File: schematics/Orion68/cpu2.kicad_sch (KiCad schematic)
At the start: 37 parts, among them J10 Conn_02x08_Counter_Clockwise, J600 Euro96pin, J601 clock, J602 clock1, Q5 2N3904, Q6 2N3904, SW1 sw_reset, U16 74LS139, U21 74LS20, U22 74HC164, U24 74HC4078, U600 68000D, U601 74LS393, U602 74HC74, U603 74HC14, U604 ATmega8-16P

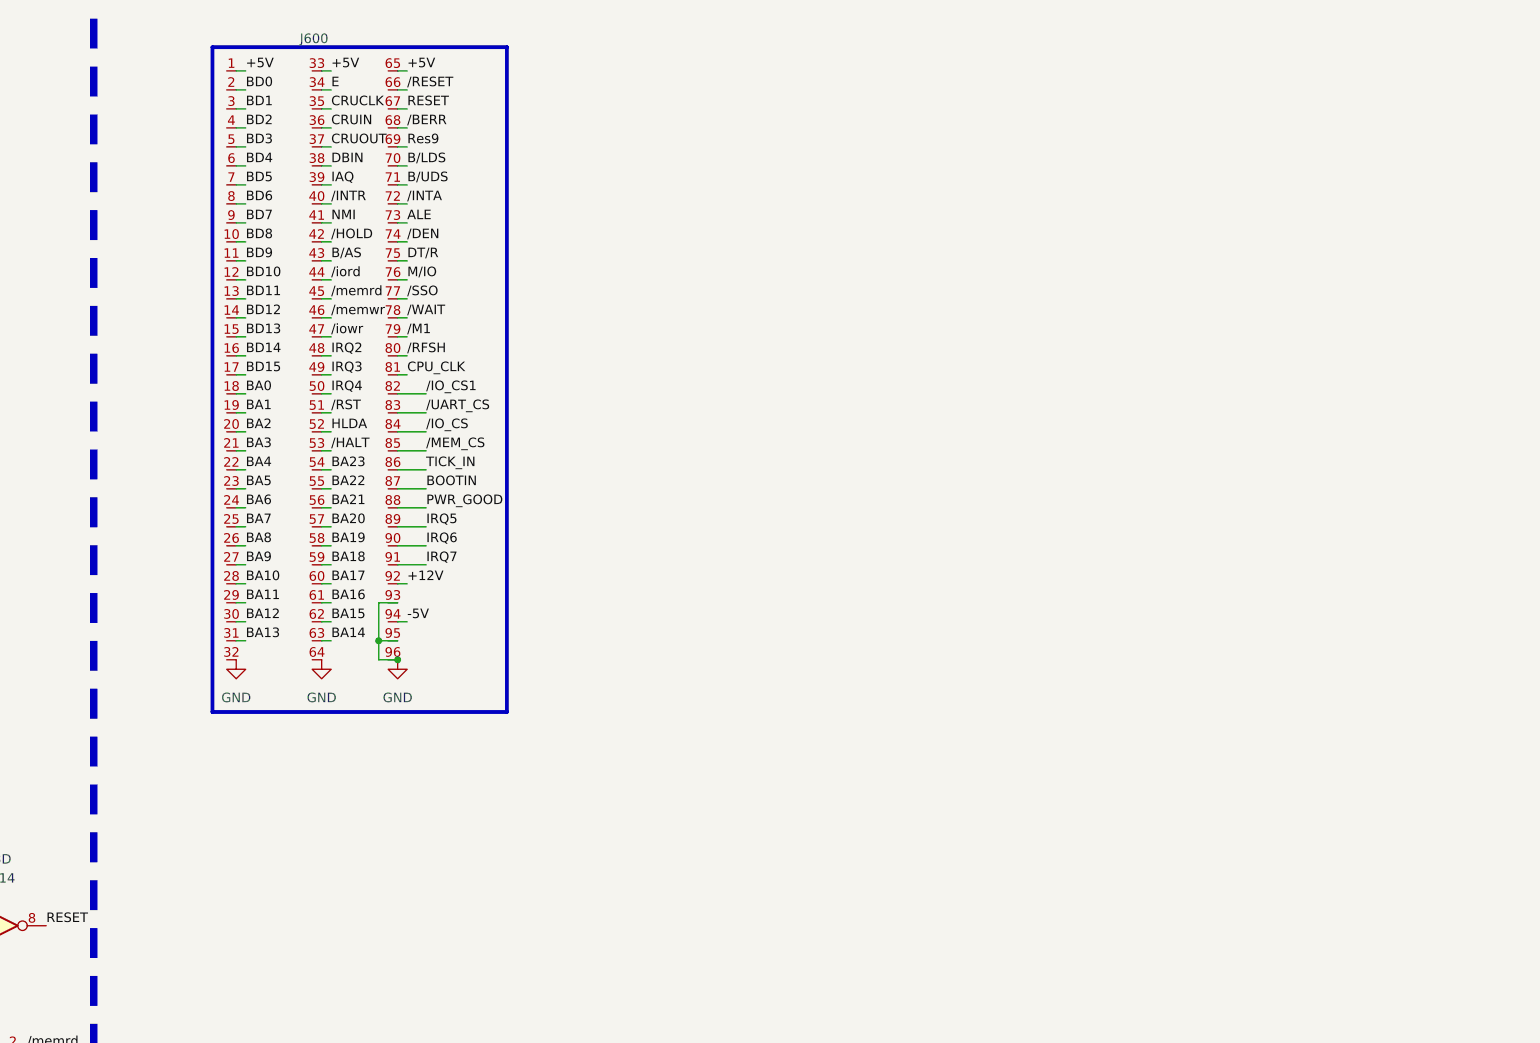
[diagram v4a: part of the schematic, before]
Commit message: B column DIN conn. all in GND
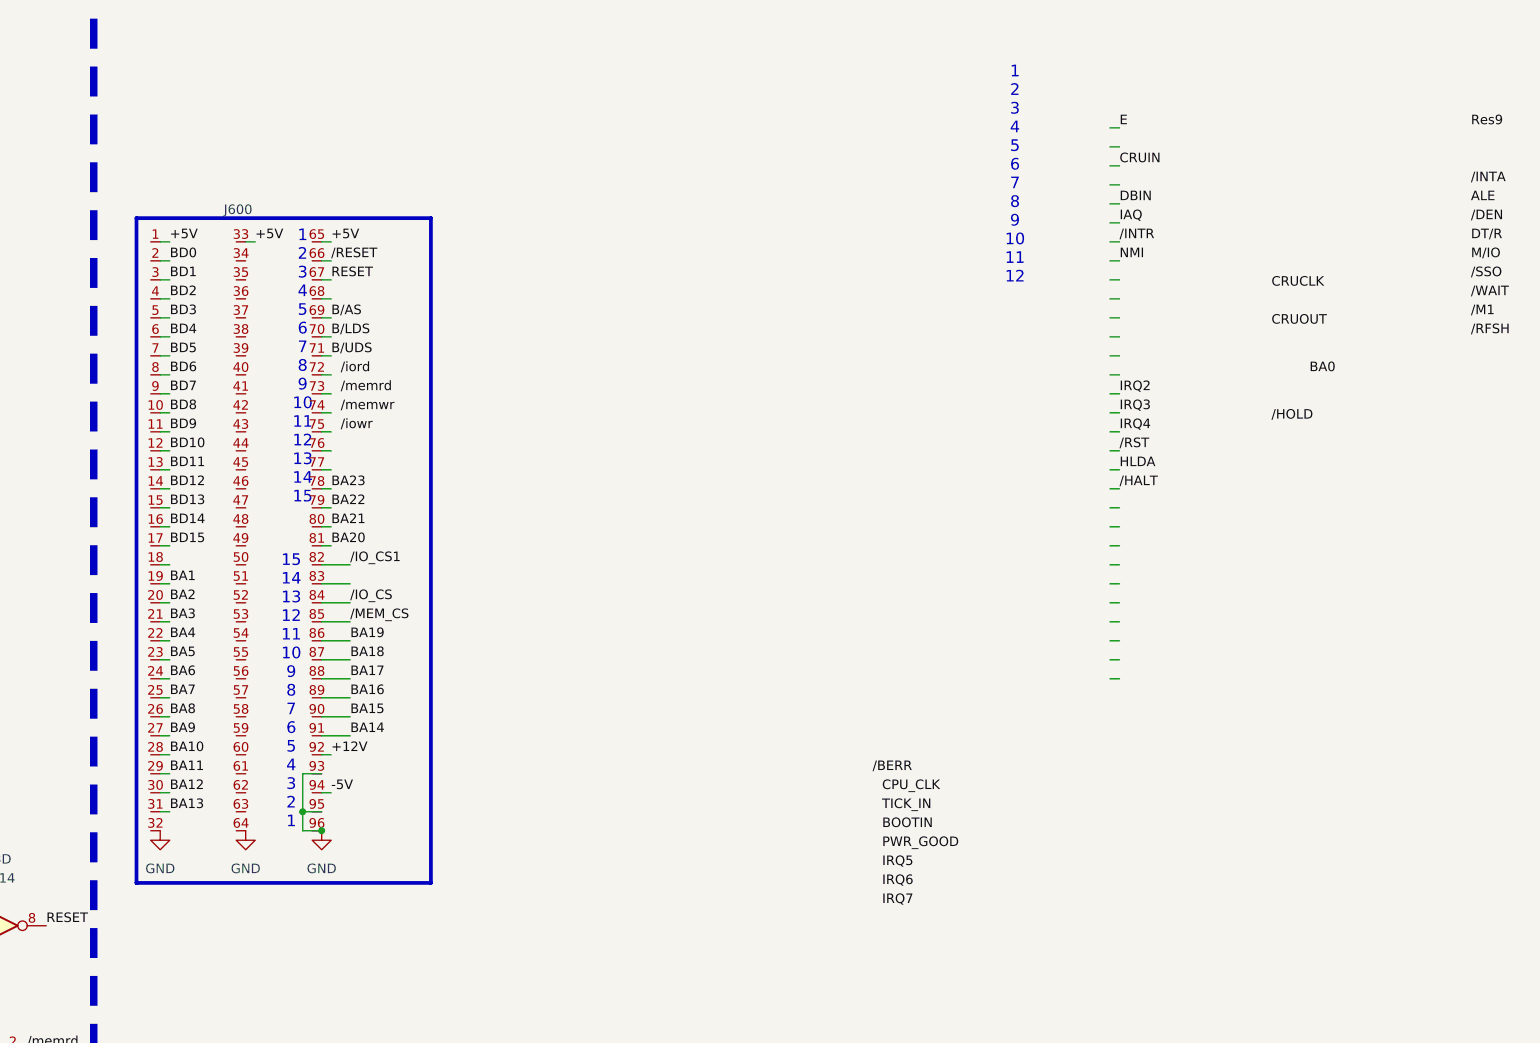
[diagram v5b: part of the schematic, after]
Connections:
- net ALE: no longer J600.73
- net BA0: no longer J600.18
- net BA14: now also J600.91; no longer J600.63
- net BA15: now also J600.90; no longer J600.62
- net BA16: now also J600.89; no longer J600.61
- net BA17: now also J600.88; no longer J600.60
- net BA18: now also J600.87; no longer J600.59
- net BA19: now also J600.86; no longer J600.58
- net BA20: now also J600.81; no longer J600.57
- net BA21: now also J600.80; no longer J600.56
- net BA22: now also J600.79; no longer J600.55
- net BA23: now also J600.78; no longer J600.54
- net BOOTIN: no longer J600.87
- net B/AS: now also J600.69; no longer J600.43
- net CPU_CLK: no longer J600.81
- net CRUCLK: no longer J600.35
- net CRUIN: no longer J600.36
- net CRUOUT: no longer J600.37
- net DBIN: no longer J600.38
- net DT/R: no longer J600.75
- net E: no longer J600.34
- net HLDA: no longer J600.52
- net IAQ: no longer J600.39
- net IRQ2: no longer J600.48
- net IRQ3: no longer J600.49
- net IRQ4: no longer J600.50
- net IRQ5: no longer J600.89
- net IRQ6: no longer J600.90
- net IRQ7: no longer J600.91
- net M/IO: no longer J600.76
- net NMI: no longer J600.41
- net PWR_GOOD: no longer J600.88
- net Res9: no longer J600.69
- net R/W: no longer J600.46
- net TICK_IN: no longer J600.86
- net /BERR: no longer J600.68
- net /DEN: no longer J600.74
- net /HALT: no longer J600.53
- net /HOLD: no longer J600.42
- net /INTA: no longer J600.72
- net /INTR: no longer J600.40
- net /M1: no longer J600.79
- net /RFSH: no longer J600.80
- net /RST: no longer J600.51
- net /SSO: no longer J600.77
- net /WAIT: no longer J600.78
- net /iord: no longer J600.44
- net /iowr: no longer J600.47
- net /memrd: no longer J600.45
- net /UART_CS: no longer names the net of J600.83
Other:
- note added: "1 2 3 4 5 6 7 8 9 10 11 12"
- note added: "1 2 3 4 5 6 7 8 9 10 11 12 13 14 15"
- note added: "15 14 13 12 11 10 9 8 7 6 5 4 3 2 1"

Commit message: just update
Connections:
- net R/W: now also J600.74
- net /iord: now also J600.72
- net /iowr: now also J600.75
- net /memrd: now also J600.73
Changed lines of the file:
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@@
 	)
 	(label "{slash}memrd"
-		(at 265.43 63.5 0)
+		(at 264.16 63.5 0)
 		(effects
 			(font
@@
 	)
 	(label "{slash}memwr"
-		(at 265.43 66.04 0)
+		(at 264.16 66.04 0)
 		(effects
 			(font
@@
 	)
 	(label "{slash}iowr"
-		(at 265.43 68.58 0)
+		(at 264.16 68.58 0)
 		(effects
 			(font
@@
 	)
 	(label "{slash}iord"
-		(at 265.43 60.96 0)
-		(effects
-			(font
+		(at 264.16 60.96 0)
+		(effects
+			(font

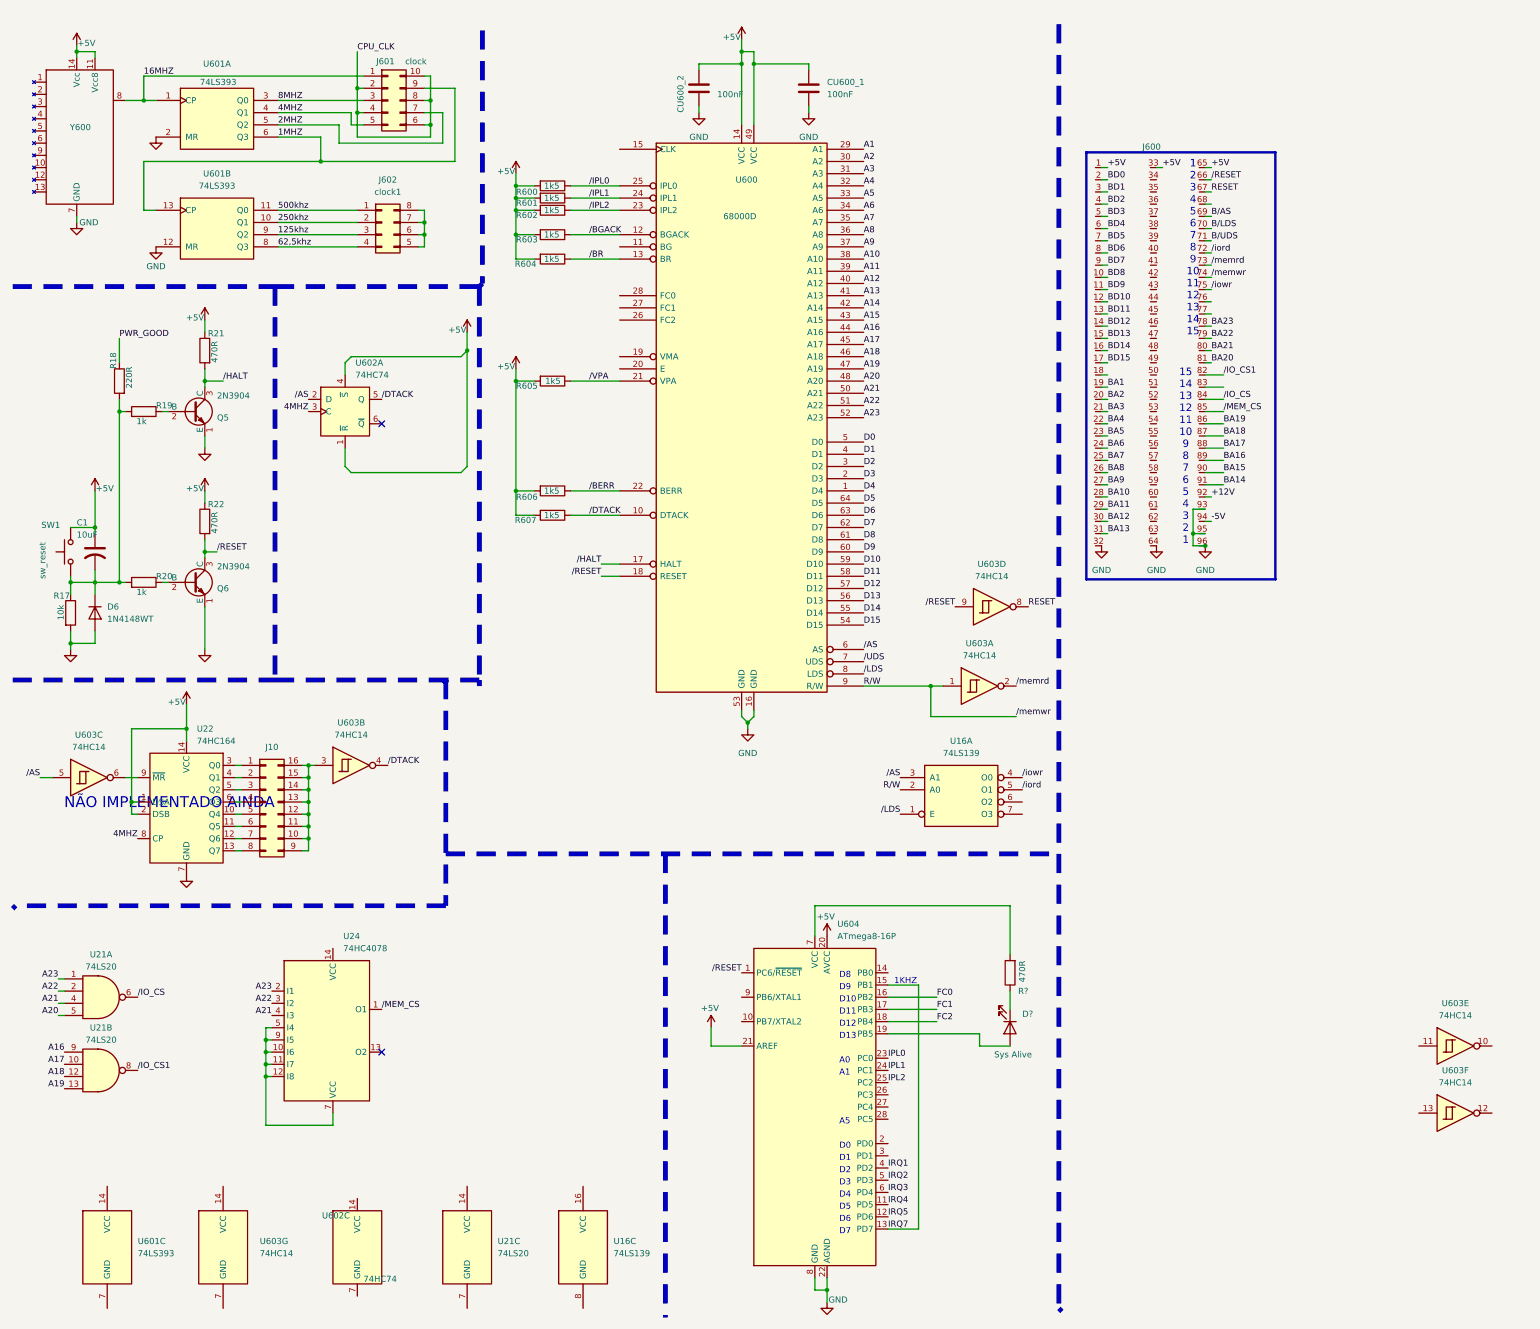
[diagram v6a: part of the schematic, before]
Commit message: New code for VBug2.0 with new reset system
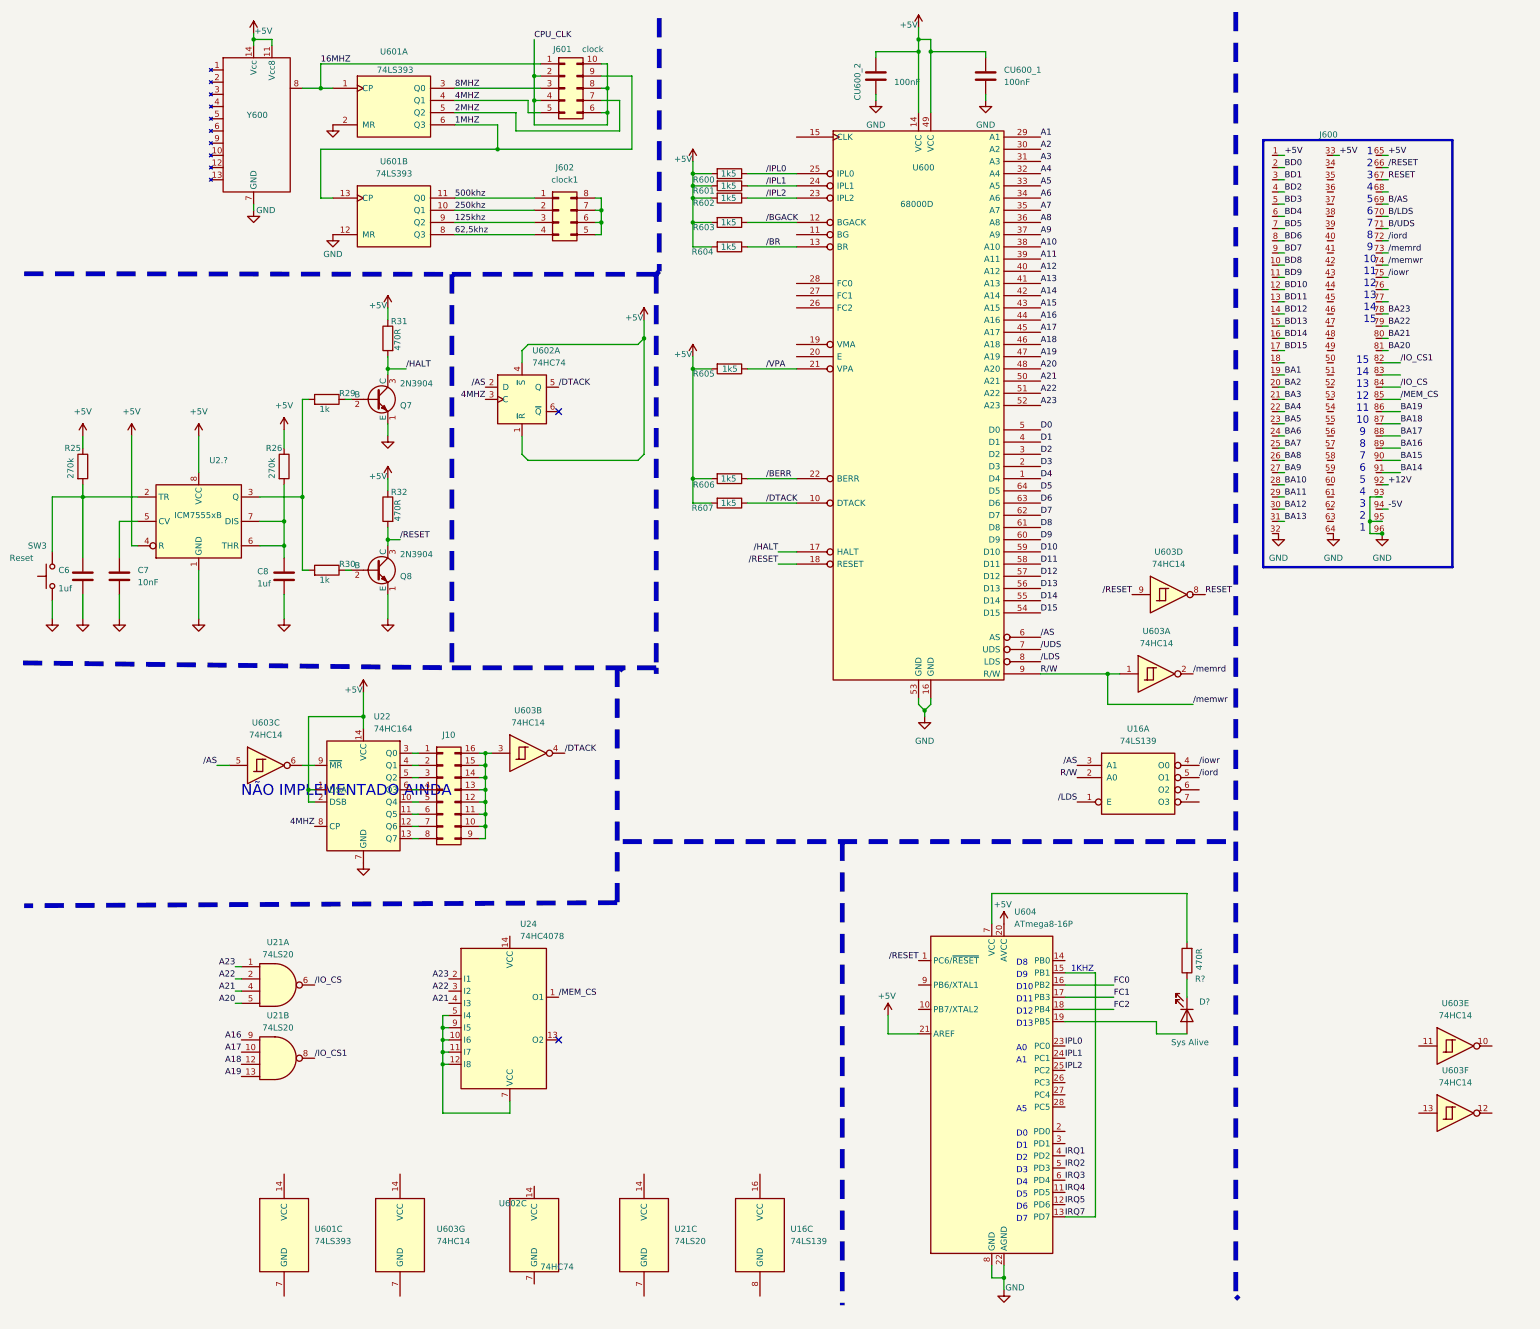
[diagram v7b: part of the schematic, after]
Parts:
- removed C1: 10uF, Capacitor_THT:CP_Radial_D5.0mm_P2.50mm, symbol Device:C_US
- removed D6: 1N4148WT, Diode_THT:D_T-1_P5.08mm_Horizontal, symbol Diode:1N4148WT
- removed Q5, Q6: 2N3904, Package_TO_SOT_THT:TO-92_Inline, symbol Transistor_BJT:2N3904
- removed R17: 10k, Resistor_THT:R_Axial_DIN0204_L3.6mm_D1.6mm_P5.08mm_Horizontal, symbol Device:R
- removed R18: 220R, Resistor_THT:R_Axial_DIN0204_L3.6mm_D1.6mm_P5.08mm_Horizontal, symbol Device:R
- removed R19, R20: 1k, Resistor_THT:R_Axial_DIN0204_L3.6mm_D1.6mm_P5.08mm_Horizontal, symbol Device:R
- removed R21, R22: 470R, Resistor_THT:R_Axial_DIN0204_L3.6mm_D1.6mm_P5.08mm_Horizontal, symbol Device:R
- removed SW1: sw_reset, Button_Switch_THT:SW_Lever_1P2T_NKK_GW12LxH, symbol Switch:SW_Push
- added C6, C8: 1uf, Capacitor_THT:CP_Radial_D8.0mm_P3.50mm, symbol Device:C
- added C7: 10nF, Capacitor_SMD:C_0603_1608Metric, symbol Device:C
- added Q7, Q8: 2N3904, Package_TO_SOT_THT:TO-92_Inline, symbol Transistor_BJT:2N3904
- added R25, R26: 270k, Resistor_THT:R_Axial_DIN0204_L3.6mm_D1.6mm_P5.08mm_Horizontal, symbol Device:R
- added R29, R30: 1k, Resistor_THT:R_Axial_DIN0204_L3.6mm_D1.6mm_P5.08mm_Horizontal, symbol Device:R
- added R31, R32: 470R, Resistor_THT:R_Axial_DIN0204_L3.6mm_D1.6mm_P5.08mm_Horizontal, symbol Device:R
- added SW3: Reset, Button_Switch_THT:SW_Push_1P2T_Vertical_E-Switch_800UDP8P1A1M6, symbol Switch:SW_Push
- added U2.?: ICM7555xB, Package_SO:SOIC-8_3.9x4.9mm_P1.27mm, symbol Timer:ICM7555xB
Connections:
- net +5V: now also R25.1, R26.1, R31.1, R32.1, U2.?.4 (R), U2.?.8 (VCC)
- net GND: now also C6.2, C7.2, C8.2, Q7.1 (E), Q8.1 (E), SW3.1, U2.?.1 (GND)
- net /HALT: now also Q7.3 (C), R31.2
- net /RESET: now also Q8.3 (C), R32.2
- new net: C6.1, R25.2, SW3.2, U2.?.2 (TR)
- new net: R29.2, R30.2, U2.?.3 (Q)
- new net: C7.1, U2.?.5 (CV)
- new net: C8.1, R26.2, U2.?.6 (THR), U2.?.7 (DIS)
- new net: Q7.2 (B), R29.1
- new net: Q8.2 (B), R30.1
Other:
- moved on the sheet: CU600_1, CU600_2, D?, J10, J600, J601, J602, R600, R601, R602, R603, R604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
